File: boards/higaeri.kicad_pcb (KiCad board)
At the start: 2 copper layers, 111.5 x 94.4 mm, 99 parts, among them J1 5051104096, J10 pot, J11 RE12A, J12 RS485_airdata, J13 Conn_01x03 speaker, J14 RE12A, J15 encoder_direct, J2 Micro_SD_Card, J3 URM37, J4 servo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

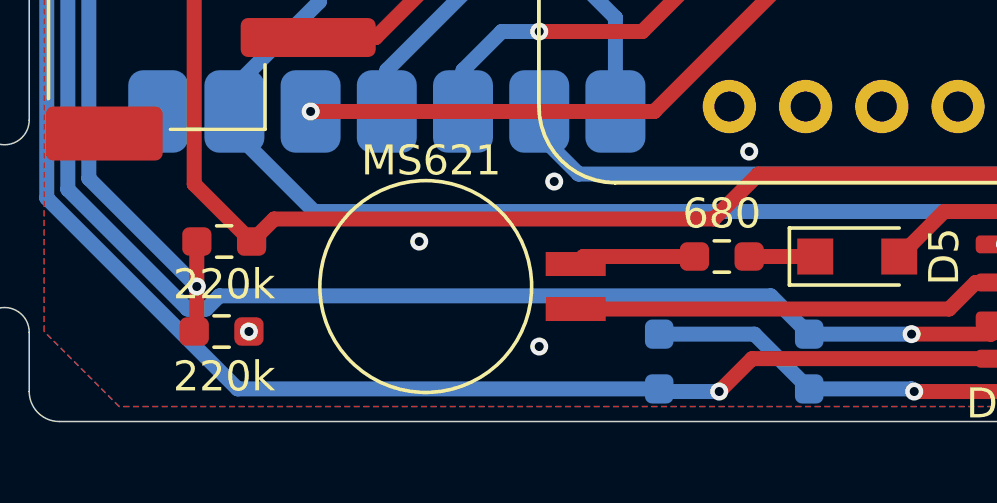
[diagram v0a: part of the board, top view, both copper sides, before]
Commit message: 高度計の補正以外完了
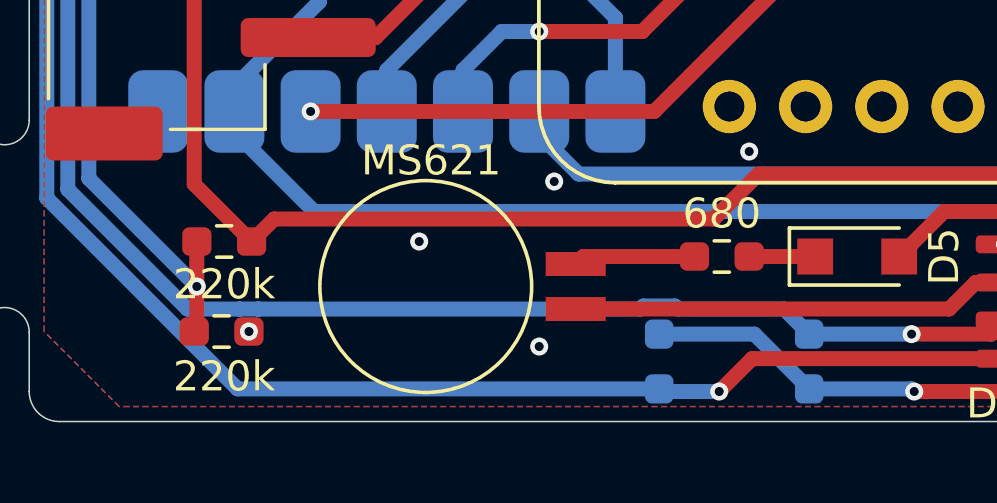
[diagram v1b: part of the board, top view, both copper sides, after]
